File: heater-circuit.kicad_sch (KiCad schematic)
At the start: 30 parts, among them U1 LM358, U2 TPS22919QDCKRQ1, U3 LM358, U4 TPS22919QDCKRQ1, U5 LM358, U6 TPS22919QDCKRQ1

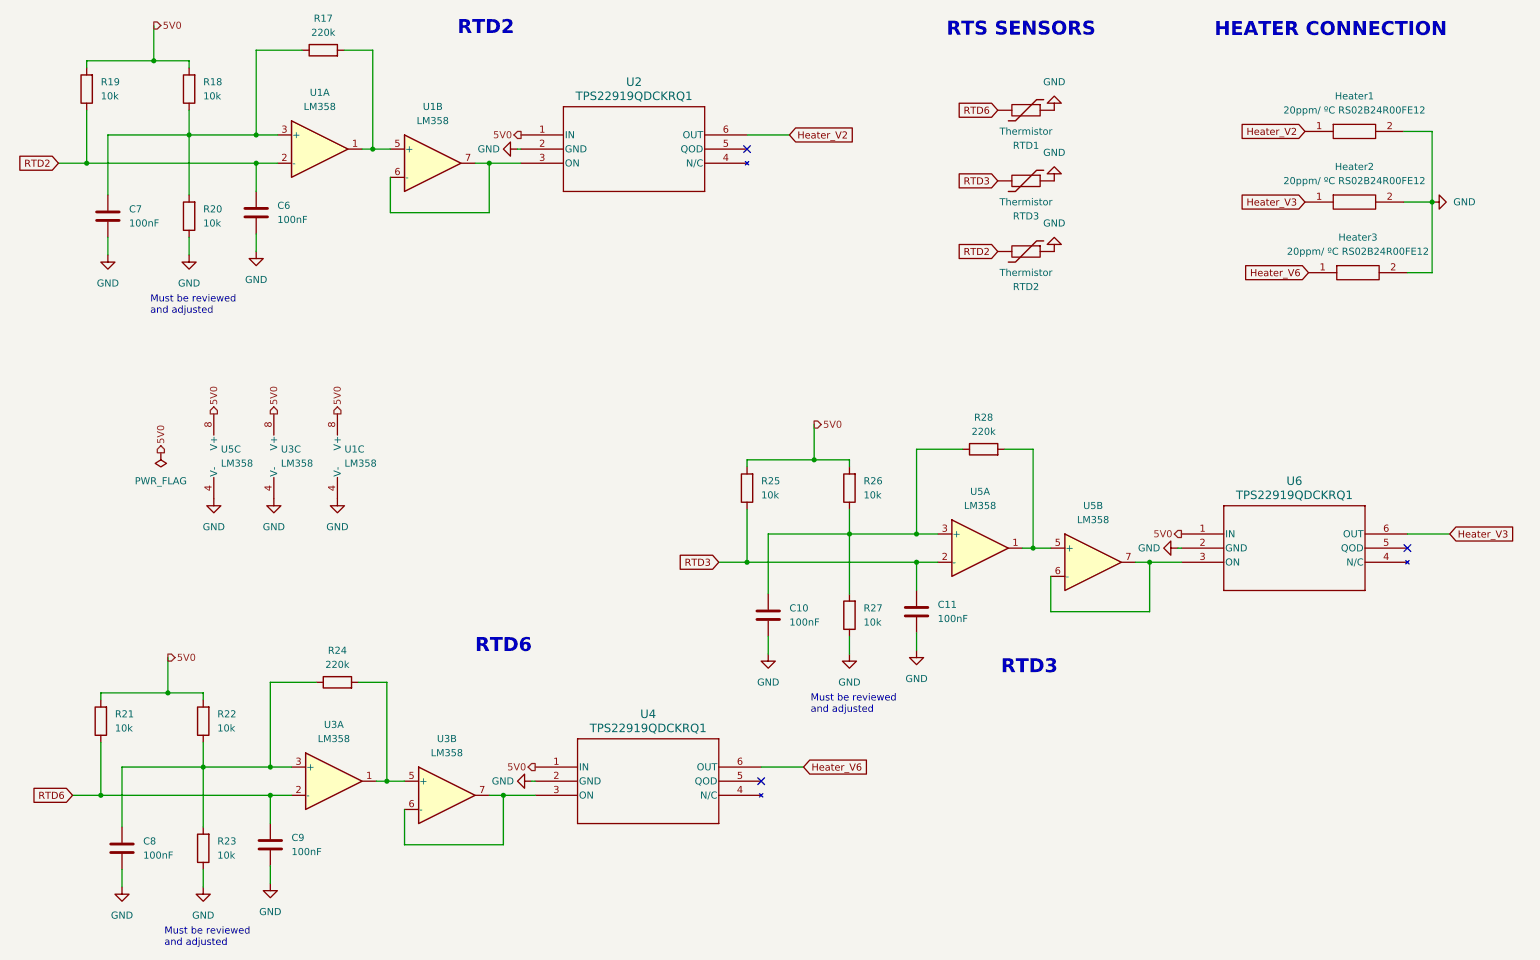
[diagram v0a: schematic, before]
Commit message: Creating hierarquical labels and organizing root
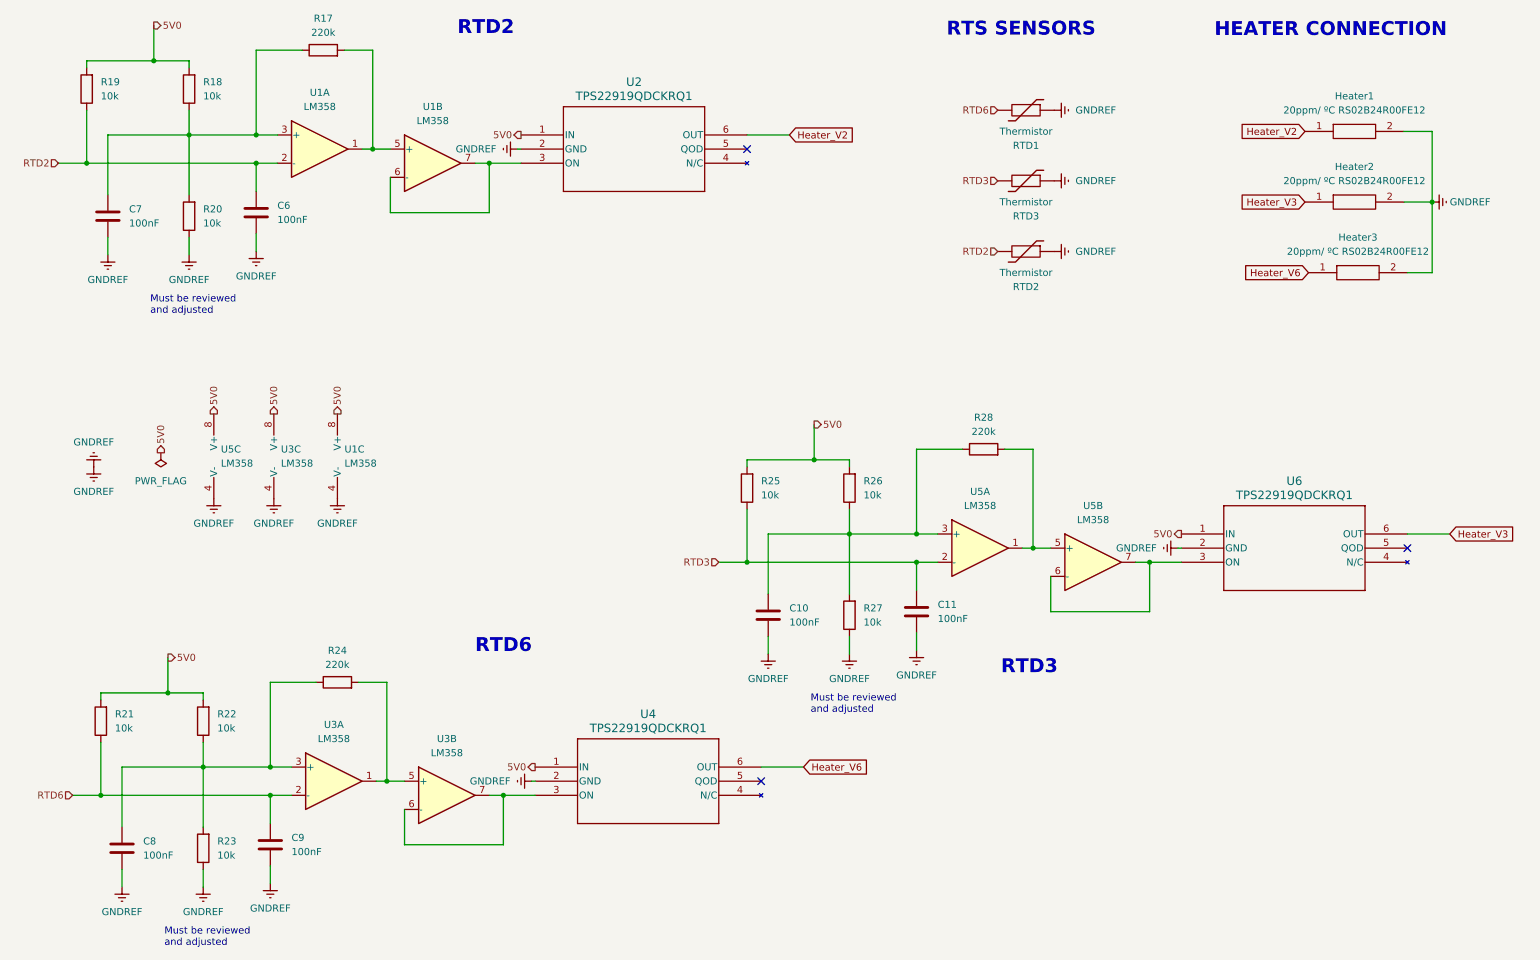
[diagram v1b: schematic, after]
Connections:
- net GND renamed GNDREF

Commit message: general improvements in schematics
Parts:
- Heater1, Heater2, Heater3: footprint lib:RS02B24R00FE12 -> footprints:RS02B24R00FE12
- RTD1, RTD2, RTD3: footprint (none) -> Resistor_SMD:R_1206_3216Metric_Pad1.30x1.75mm_HandSolder
- U1, U3, U5: footprint (none) -> Package_SO:SOIC-8_3.9x4.9mm_P1.27mm; Partnumber (none) -> LM358BIDR
- U2, U4, U6: footprint lib:TPS22919QDCKRQ1 -> footprints:TPS22919QDCKRQ1
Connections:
- net 5V0 renamed 3V3
